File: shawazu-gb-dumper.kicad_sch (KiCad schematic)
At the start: 16 parts, among them J1 GB_CART, SW1 VSEL, U1 BOB-12009, U2 BOB-12009, U3 BOB-12009, U4 BOB-12009, U5 BOB-12009, U6 BOB-12009, U7 BOB-12009, U8 Pico

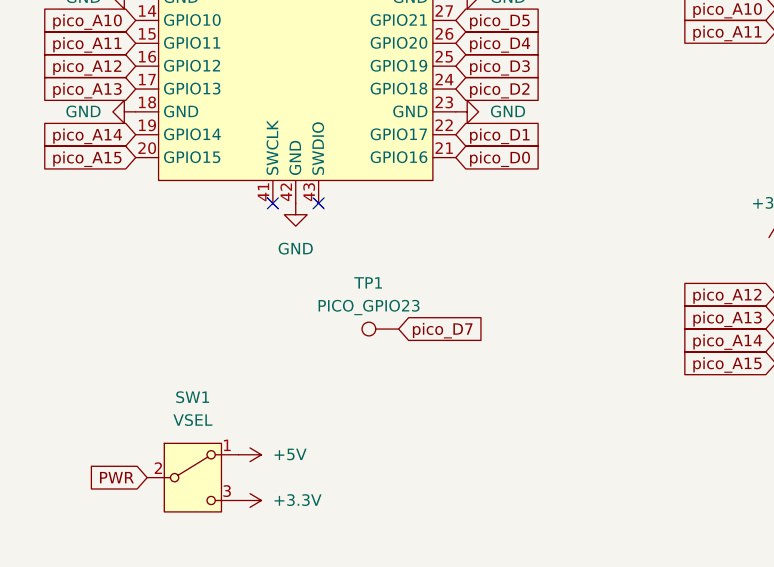
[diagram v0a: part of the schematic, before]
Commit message: Update shawazu-gb-dumper.kicad_sch
Tp4
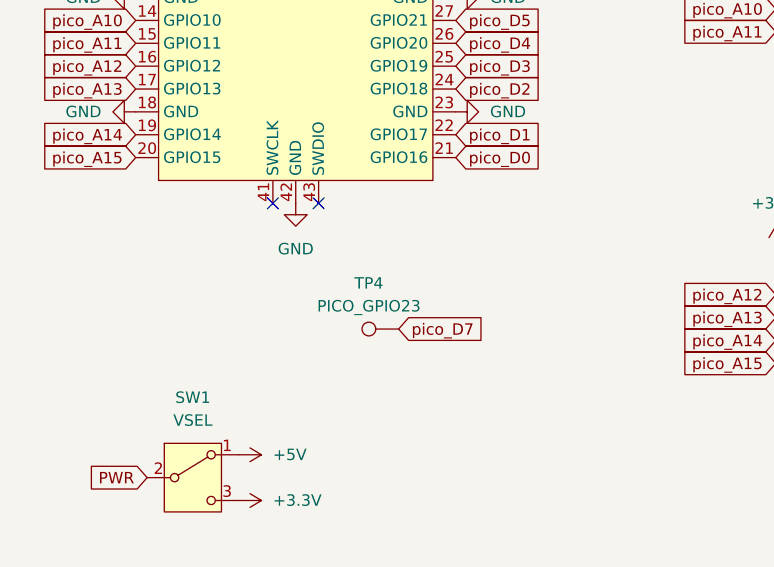
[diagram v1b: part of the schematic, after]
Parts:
- renumbered TP1 to TP4
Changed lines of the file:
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@@
 		(dnp no)
 		(fields_autoplaced yes)
-		(property "Reference" "TP1"
+		(property "Reference" "TP4"
 			(at 58.928 119.38 90)
 			(effects
@@
 			(project "shawazu-gb-dumper"
 				(path "/97e0a329-8697-49bc-b4ba-9c706c6dd8be"
-					(reference "TP1")
+					(reference "TP4")
 					(unit 1)
 				)
